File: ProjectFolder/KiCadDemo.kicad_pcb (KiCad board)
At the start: 2 copper layers, 24 parts, among them J1 1992, J2 TSW-103-07-T-S, J3 TSW-103-07-T-S, J4 TSW-103-07-T-S, J5 TSW-103-07-T-S, J6 TSW-103-07-T-S, J7 TSW-103-07-T-S, U1 SN74LVC1G139DCTR, U2 SN74LVC1G139DCTR, U3 SN74LVC1G139DCTR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

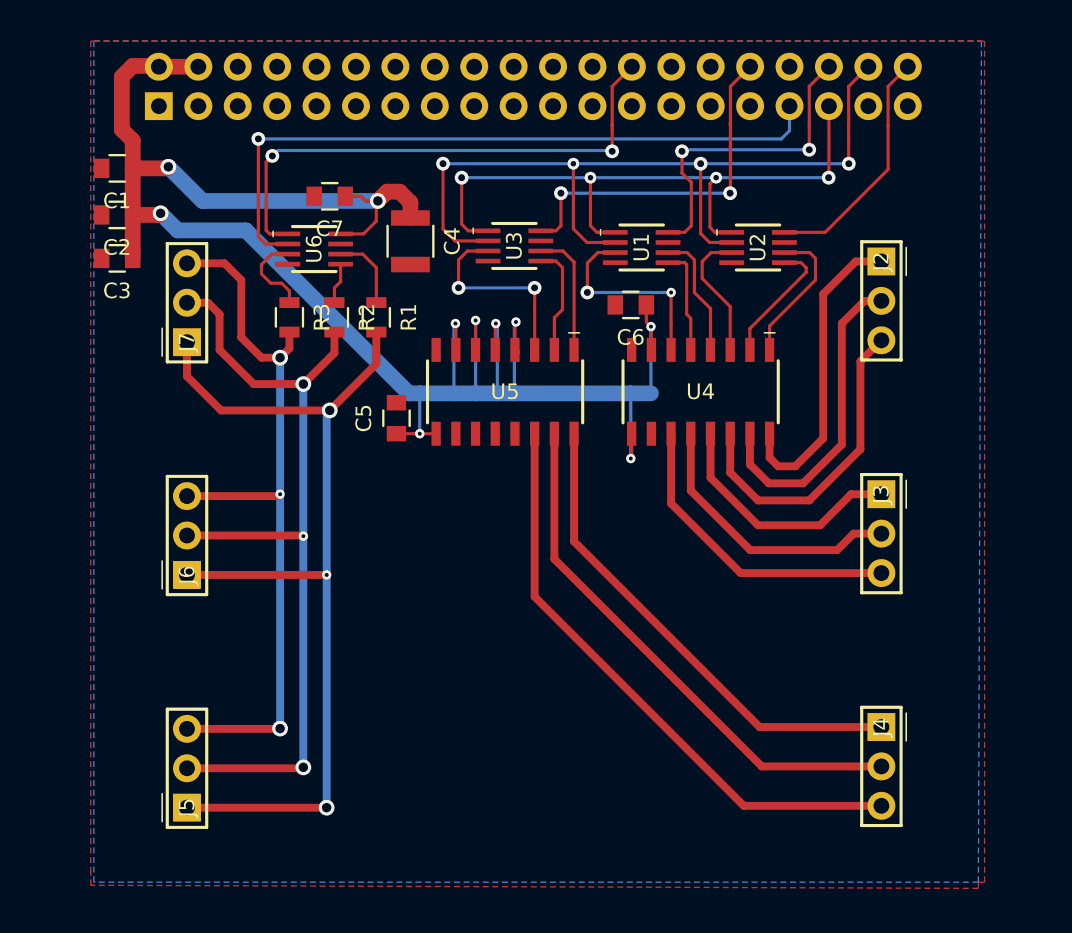
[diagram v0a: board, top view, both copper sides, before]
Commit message: Added mounting holes, fixed Raspberry Pi reference footprint mounting hole locations, and removed inaccurate mechanical drawing
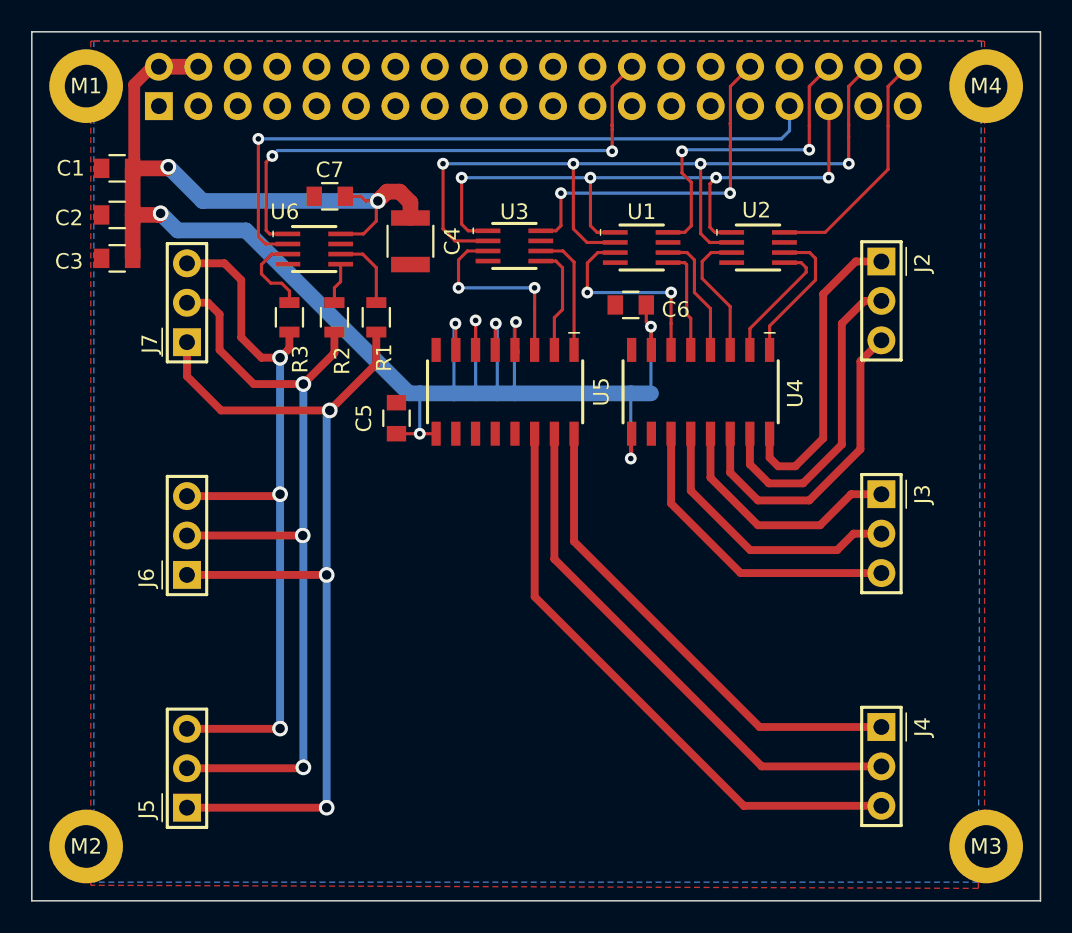
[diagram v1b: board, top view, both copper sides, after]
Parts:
- added M1: Mounting_Hole, mounting_hole:mounting_hole_2.75mm_pth, F.Cu at (63.5, 73.5)
- added M2: Mounting_Hole, mounting_hole:mounting_hole_2.75mm_pth, F.Cu at (63.5, 122.5)
- added M3: Mounting_Hole, mounting_hole:mounting_hole_2.75mm_pth, F.Cu at (121.5, 122.5)
- added M4: Mounting_Hole, mounting_hole:mounting_hole_2.75mm_pth, F.Cu at (121.5, 73.5)
- raspberrypi2_shield: footprint raspberrypi2_shield:raspberrypi2_shield -> raspberrypi2_shield
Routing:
- net +5V: track 126.9 -> 125.6 mm
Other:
- board outline added: 65 x 56 mm

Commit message: branch to store exercise project, remove mounting holes including libraries
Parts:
- removed M1, M2, M3, M4: Mounting_Hole, mounting_hole:mounting_hole_2.75mm_pth
